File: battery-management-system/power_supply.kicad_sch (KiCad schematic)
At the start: 0 parts

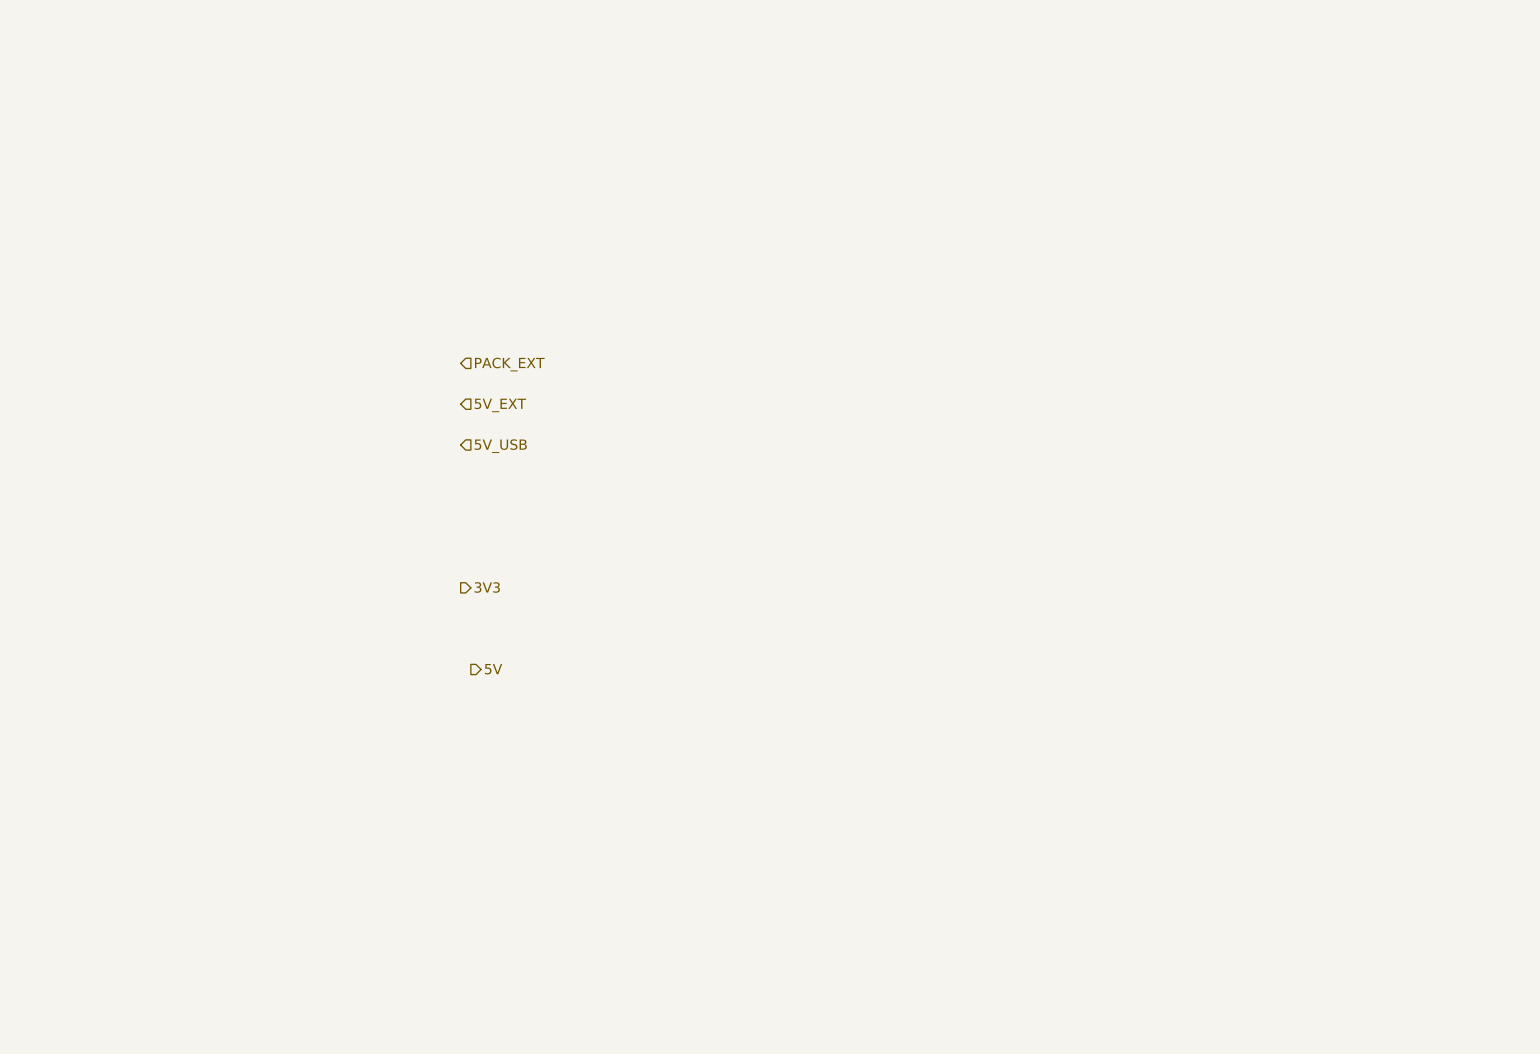
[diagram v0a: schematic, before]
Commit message: define basic hierarchy and power supplies
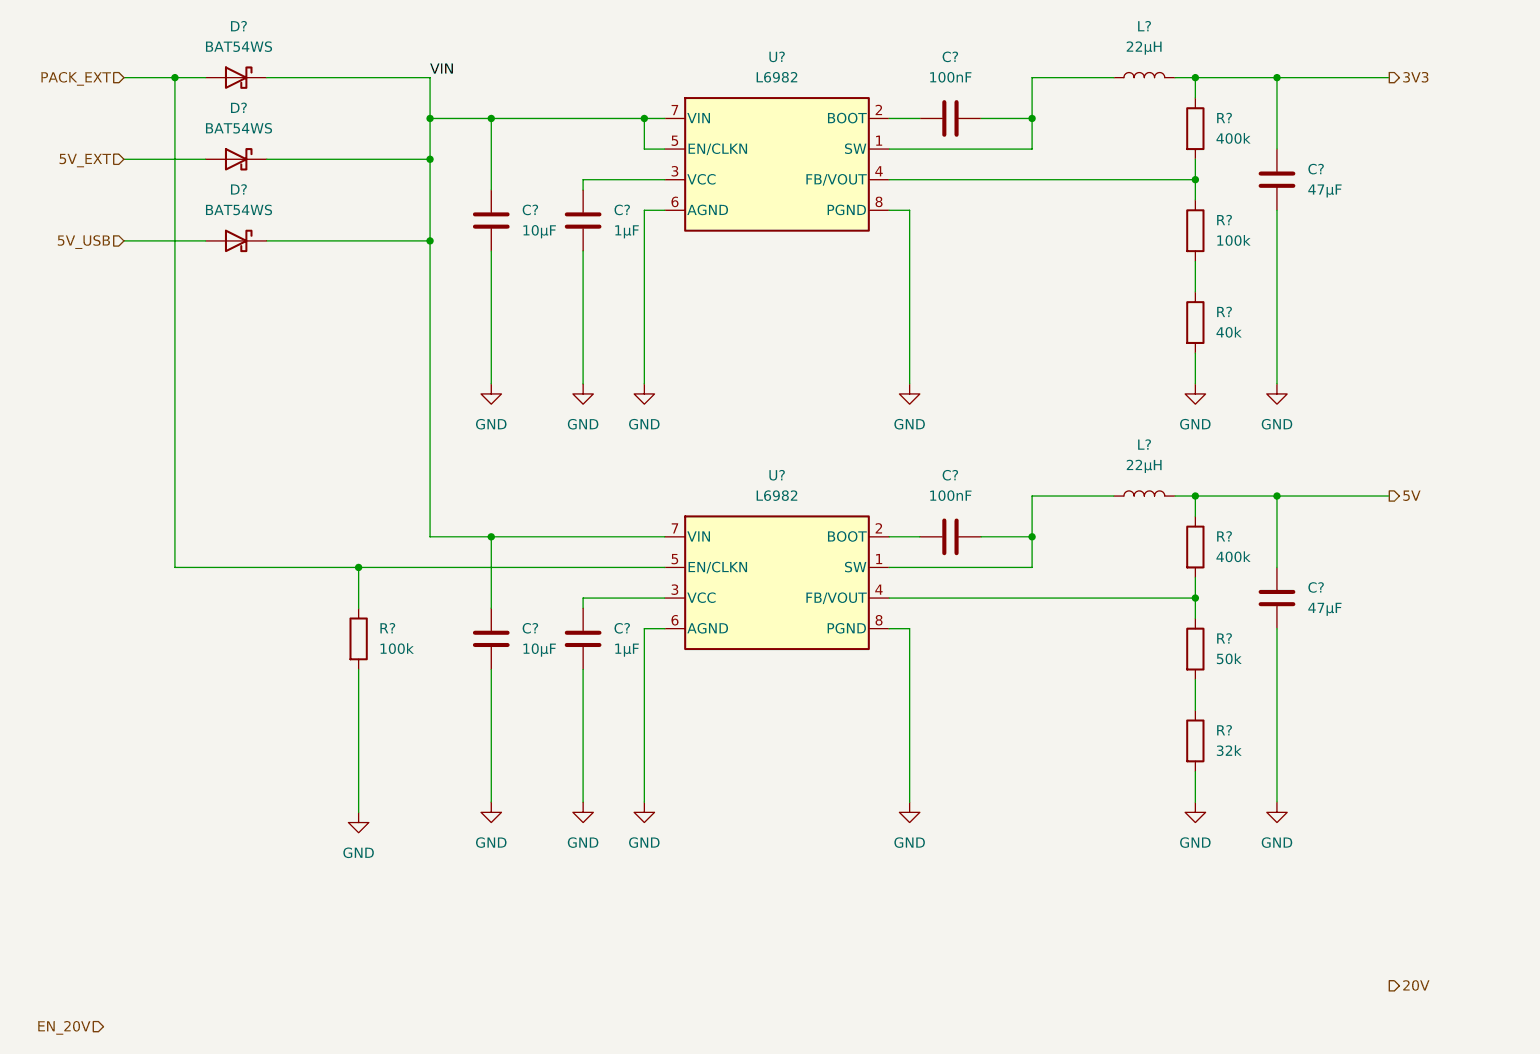
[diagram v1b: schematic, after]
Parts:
- added C? (x2): 100nF, symbol Device:C
- added C? (x2): 47µF, symbol Device:C
- added C? (x2): 10µF, symbol Device:C
- added C? (x2): 1µF, symbol Device:C
- added D? (x3): BAT54WS, Diode_SMD:D_SOD-323, symbol benediktibk:BAT54WS
- added L? (x2): 22µH, symbol Device:L
- added R?: 32k, symbol Device:R
- added R? (x2): 100k, symbol Device:R
- added R? (x2): 400k, symbol Device:R
- added R?: 50k, symbol Device:R
- added R?: 40k, symbol Device:R
- added U? (x2): L6982, Package_SO:SO-8_3.9x4.9mm_P1.27mm, symbol benediktibk:L6982
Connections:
- net 3V3: now also C?.1, L?.1, R?.1
- net 5V: now also C?.1, L?.1, R?.1
- net 5V_EXT: now also D?.2 (A)
- net 5V_USB: now also D?.2 (A)
- net PACK_EXT: now also D?.2 (A), R?.1, U?.5 (EN/CLKN)
- new net: R?.1, R?.2 (x2)
- new net: C?.1, L?.2, U?.1 (SW) (x2)
- new net: C?.2, U?.2 (BOOT) (x2)
- new net: C?.1, U?.3 (VCC) (x2)
- new net: R?.1, R?.2, U?.4 (FB/VOUT) (x2)
- new net GND: C?.2, C?.2, C?.2, C?.2, C?.2, C?.2, R?.2, R?.2, R?.2, U?.6 (AGND), U?.6 (AGND), U?.8 (PGND), U?.8 (PGND)
- new net VIN: C?.1, C?.1, D?.1 (K), D?.1 (K), D?.1 (K), U?.5 (EN/CLKN), U?.7 (VIN), U?.7 (VIN)

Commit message: enable 5V with VIN
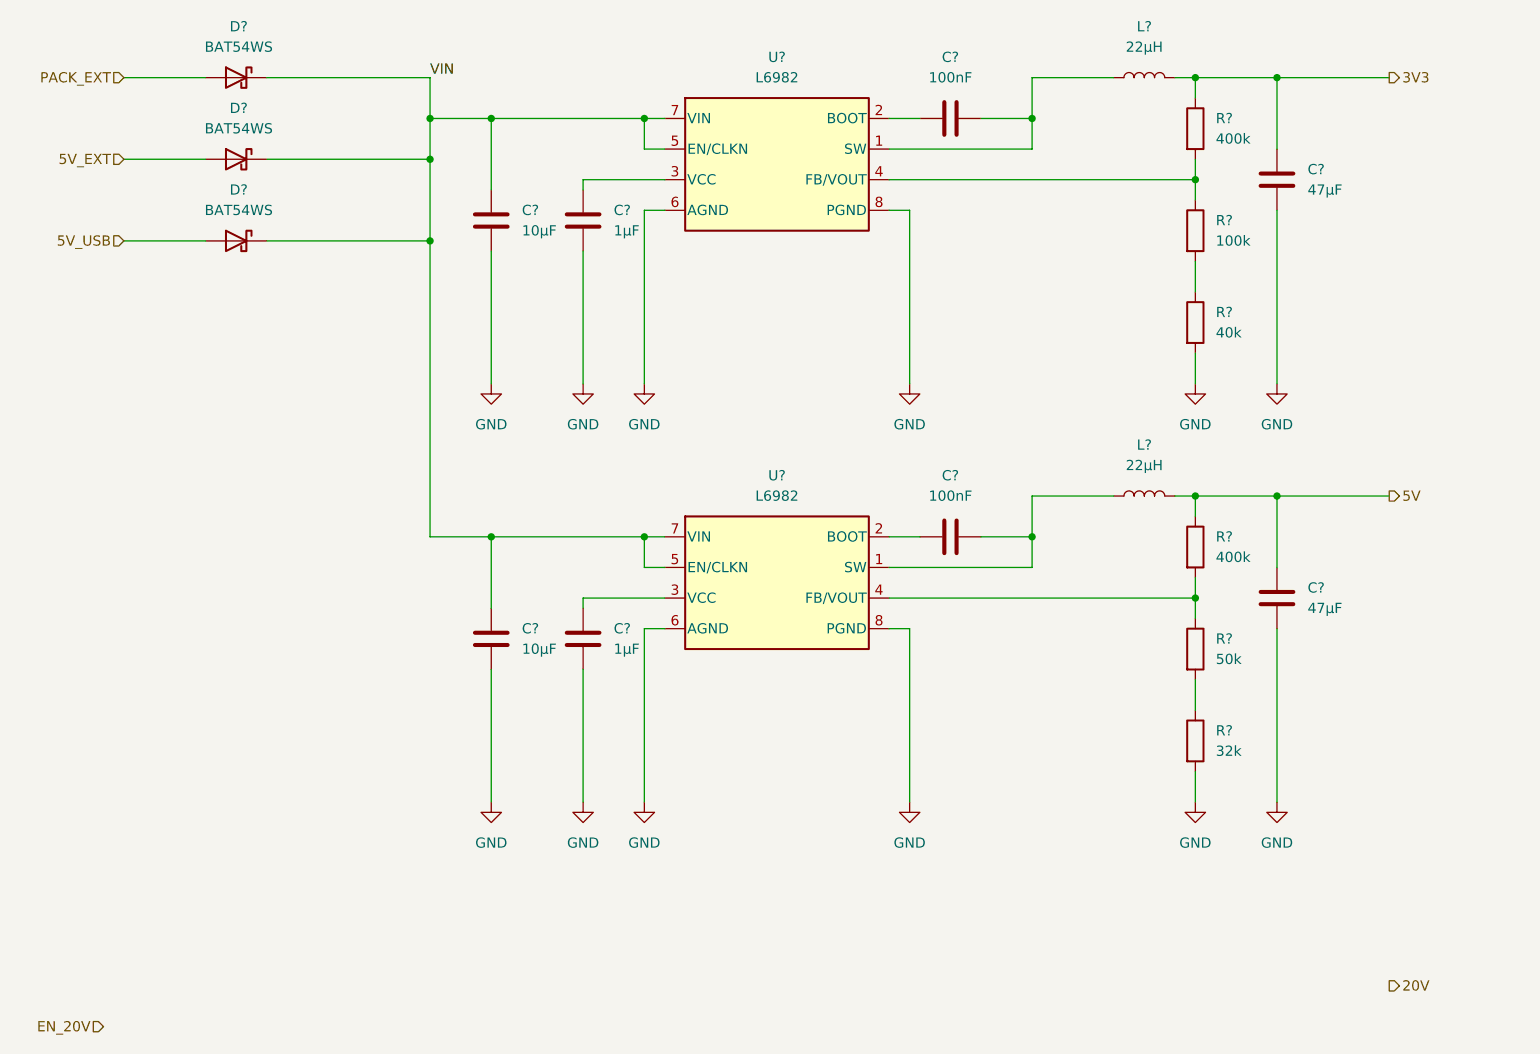
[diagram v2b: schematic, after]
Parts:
- removed R?: 100k, symbol Device:R
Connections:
- net PACK_EXT: no longer U?.5 (EN/CLKN)
- net VIN: now also U?.5 (EN/CLKN)
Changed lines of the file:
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@@
   (junction (at 162.56 85.09) (diameter 0) (color 0 0 0 0)
   )
-  (junction (at 35.56 20.32) (diameter 0) (color 0 0 0 0)
+  (junction (at 93.98 77.47) (diameter 0) (color 0 0 0 0)
   )
   (junction (at 93.98 25.4) (diameter 0) (color 0 0 0 0)
@@
   (junction (at 67.31 30.48) (diameter 0) (color 0 0 0 0)
   )
-  (junction (at 58.42 81.28) (diameter 0) (color 0 0 0 0)
-  )
   (wire (pts (xy 86.36 41.91) (xy 86.36 58.42))
     (stroke (width 0) (type default) (color 0 0 0 0))
@@
     (stroke (width 0) (type default) (color 0 0 0 0))
   )
-  (wire (pts (xy 29.21 20.32) (xy 35.56 20.32))
+  (wire (pts (xy 29.21 20.32) (xy 39.37 20.32))
     (stroke (width 0) (type default) (color 0 0 0 0))
   )
@@
     (stroke (width 0) (type default) (color 0 0 0 0))
   )
+  (wire (pts (xy 96.52 81.28) (xy 93.98 81.28))
+    (stroke (width 0) (type default) (color 0 0 0 0))
+  )
   (wire (pts (xy 172.72 88.9) (xy 172.72 110.49))
     (stroke (width 0) (type default) (color 0 0 0 0))
@@
     (stroke (width 0) (type default) (color 0 0 0 0))
   )
-  (wire (pts (xy 58.42 93.98) (xy 58.42 111.76))
-    (stroke (width 0) (type default) (color 0 0 0 0))
-  )
   (wire (pts (xy 172.72 81.28) (xy 172.72 72.39))
     (stroke (width 0) (type default) (color 0 0 0 0))
   )
-  (wire (pts (xy 35.56 20.32) (xy 39.37 20.32))
-    (stroke (width 0) (type default) (color 0 0 0 0))
-  )
   (wire (pts (xy 96.52 88.9) (xy 93.98 88.9))
     (stroke (width 0) (type default) (color 0 0 0 0))
@@
     (stroke (width 0) (type default) (color 0 0 0 0))
   )
-  (wire (pts (xy 35.56 81.28) (xy 58.42 81.28))
-    (stroke (width 0) (type default) (color 0 0 0 0))
-  )
   (wire (pts (xy 160.02 72.39) (xy 162.56 72.39))
     (stroke (width 0) (type default) (color 0 0 0 0))
@@
     (stroke (width 0) (type default) (color 0 0 0 0))
   )
-  (wire (pts (xy 74.93 77.47) (xy 96.52 77.47))
+  (wire (pts (xy 74.93 77.47) (xy 93.98 77.47))
     (stroke (width 0) (type default) (color 0 0 0 0))
   )
@@
     (stroke (width 0) (type default) (color 0 0 0 0))
   )
-  (wire (pts (xy 58.42 81.28) (xy 58.42 86.36))
-    (stroke (width 0) (type default) (color 0 0 0 0))
-  )
   (wire (pts (xy 124.46 81.28) (xy 142.24 81.28))
     (stroke (width 0) (type default) (color 0 0 0 0))
   )
-  (wire (pts (xy 58.42 81.28) (xy 96.52 81.28))
+  (wire (pts (xy 93.98 77.47) (xy 96.52 77.47))
     (stroke (width 0) (type default) (color 0 0 0 0))
   )
@@
     (stroke (width 0) (type default) (color 0 0 0 0))
   )
-  (wire (pts (xy 35.56 20.32) (xy 35.56 81.28))
-    (stroke (width 0) (type default) (color 0 0 0 0))
-  )
   (wire (pts (xy 29.21 40.64) (xy 39.37 40.64))
     (stroke (width 0) (type default) (color 0 0 0 0))
@@
   )
   (wire (pts (xy 96.52 25.4) (xy 93.98 25.4))
+    (stroke (width 0) (type default) (color 0 0 0 0))
+  )
+  (wire (pts (xy 93.98 81.28) (xy 93.98 77.47))
     (stroke (width 0) (type default) (color 0 0 0 0))
   )
@@
     )
     (pin "1")
-  )
-  (symbol (lib_id "Device:R") (at 58.42 90.17 0) (unit 1)
-    (in_bom yes) (on_board yes) (fields_autoplaced)
-    (property "Reference" "R?" (id 0) (at 60.96 88.8999 0)
-      (effects (font (size 1.27 1.27)) (justify left))
-    )
-    (property "Value" "100k" (id 1) (at 60.96 91.4399 0)
-      (effects (font (size 1.27 1.27)) (justify left))
-    )
-    (property "Footprint" "" (id 2) (at 56.642 90.17 90)
-      (effects (font (size 1.27 1.27)) hide)
-    )
-    (property "Datasheet" "~" (id 3) (at 58.42 90.17 0)
-      (effects (font (size 1.27 1.27)) hide)
-    )
-    (pin "1")
-    (pin "2")
   )
   (symbol (lib_id "Device:C") (at 172.72 33.02 0) (unit 1)
@@
       (effects (font (size 1.27 1.27)) hide)
     )
-    (pin "1")
-  )
-  (symbol (lib_id "power:GND") (at 58.42 111.76 0) (unit 1)
-    (in_bom yes) (on_board yes) (fields_autoplaced)
-    (property "Reference" "#PWR?" (id 0) (at 58.42 118.11 0)
-      (effects (font (size 1.27 1.27)) hide)
-    )
-    (property "Value" "GND" (id 1) (at 58.42 116.84 0))
-    (property "Footprint" "" (id 2) (at 58.42 111.76 0)
-      (effects (font (size 1.27 1.27)) hide)
-    )
-    (property "Datasheet" "" (id 3) (at 58.42 111.76 0)
-      (effects (font (size 1.27 1.27)) hide)
-    )

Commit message: add RS order numbers
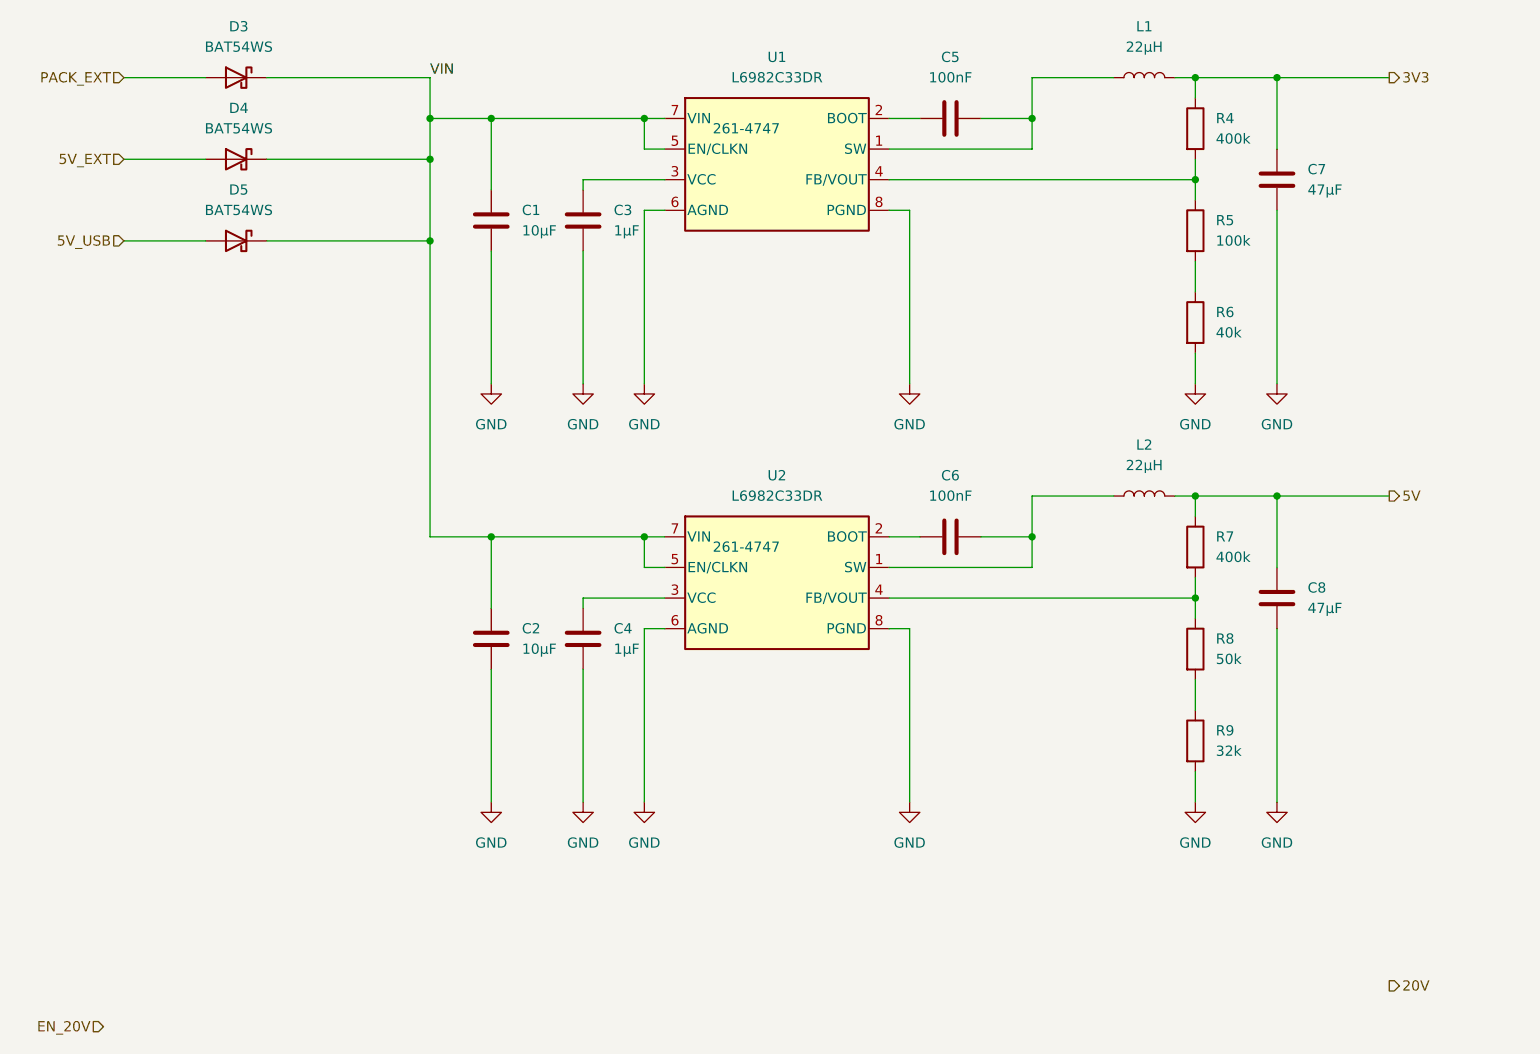
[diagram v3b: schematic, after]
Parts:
- D3, D4, D5: renamed from D?; RS order number (none) -> 738-4844
- U1, U2: renamed from U?; value L6982 -> L6982C33DR; symbol benediktibk:L6982 -> benediktibk:L6982C33DR; RS order number (none) -> 261-4747
- gave numbers to parts that had none: 16

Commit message: use own symbols and footprints
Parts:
- D3, D4, D5: footprint Diode_SMD:D_SOD-323 -> benediktibk:D_SOD-323
- U1, U2: footprint Package_SO:SO-8_3.9x4.9mm_P1.27mm -> benediktibk:SO-8_3.9x4.9mm_P1.27mm
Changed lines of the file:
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@@
     (pin "1")
   )
-  (symbol (lib_id "benediktibk:L6982C33DR") (at 106.68 26.67 0) (unit 1)
+  (symbol (lib_name "L6982C33DR_1") (lib_id "benediktibk:L6982C33DR") (at 106.68 26.67 0) (unit 1)
     (in_bom yes) (on_board yes) (fields_autoplaced)
     (property "Reference" "U1" (id 0) (at 110.49 17.78 0))
     (property "Value" "L6982C33DR" (id 1) (at 110.49 20.32 0))
-    (property "Footprint" "Package_SO:SO-8_3.9x4.9mm_P1.27mm" (id 2) (at 106.68 19.05 0)
+    (property "Footprint" "benediktibk:SO-8_3.9x4.9mm_P1.27mm" (id 2) (at 106.68 19.05 0)
       (effects (font (size 1.27 1.27)) hide)
     )
@@
     (property "Reference" "D3" (id 0) (at 43.4975 13.97 0))
     (property "Value" "BAT54WS" (id 1) (at 43.4975 16.51 0))
-    (property "Footprint" "Diode_SMD:D_SOD-323" (id 2) (at 43.18 20.32 0)
+    (property "Footprint" "benediktibk:D_SOD-323" (id 2) (at 43.18 20.32 0)
       (effects (font (size 1.27 1.27)) hide)
     )
@@
     (pin "2")
   )
-  (symbol (lib_id "benediktibk:BAT54WS") (at 43.18 40.64 0) (mirror y) (unit 1)
+  (symbol (lib_name "BAT54WS_2") (lib_id "benediktibk:BAT54WS") (at 43.18 40.64 0) (mirror y) (unit 1)
     (in_bom yes) (on_board yes) (fields_autoplaced)
     (property "Reference" "D5" (id 0) (at 43.4975 34.29 0))
     (property "Value" "BAT54WS" (id 1) (at 43.4975 36.83 0))
-    (property "Footprint" "Diode_SMD:D_SOD-323" (id 2) (at 43.18 40.64 0)
+    (property "Footprint" "benediktibk:D_SOD-323" (id 2) (at 43.18 40.64 0)
       (effects (font (size 1.27 1.27)) hide)
     )
@@
     (property "Reference" "U2" (id 0) (at 110.49 69.85 0))
     (property "Value" "L6982C33DR" (id 1) (at 110.49 72.39 0))
-    (property "Footprint" "Package_SO:SO-8_3.9x4.9mm_P1.27mm" (id 2) (at 106.68 71.12 0)
+    (property "Footprint" "benediktibk:SO-8_3.9x4.9mm_P1.27mm" (id 2) (at 106.68 71.12 0)
       (effects (font (size 1.27 1.27)) hide)
     )
@@
     (pin "2")
   )
-  (symbol (lib_id "benediktibk:BAT54WS") (at 43.18 30.48 0) (mirror y) (unit 1)
+  (symbol (lib_name "BAT54WS_1") (lib_id "benediktibk:BAT54WS") (at 43.18 30.48 0) (mirror y) (unit 1)
     (in_bom yes) (on_board yes) (fields_autoplaced)
     (property "Reference" "D4" (id 0) (at 43.4975 24.13 0))
     (property "Value" "BAT54WS" (id 1) (at 43.4975 26.67 0))
-    (property "Footprint" "Diode_SMD:D_SOD-323" (id 2) (at 43.18 30.48 0)
-      (effects (font (size 1.27 1.27)) hide)
-    )
+    (property "Footprint" "benediktibk:D_SOD-323" (id 2) (at 43.18 30.48 0)
+      (effects (font (size 1.27 1.27)) hide)
+    )
